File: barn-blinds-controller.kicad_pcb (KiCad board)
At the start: 4 copper layers, 65 x 60 mm, 85 parts, among them J1 DC005-T20, J2 KH-TYPE-C-16P (Kinghelm), J3 Conn_01x08, J4 Conn_01x05, SW1 RESET, SW2 BOOT, U1 DCDC Converter, U10 TMP235, U11 ACS723xLCTR-05AB, U2 AP2112K-3.3, U3 ESP32-S3-WROOM-1, U4 ISO7760DBQ, U5 ISO7760DBQ, U6 ISO7760DBQ, U7 AMS1117-3.3, U8 TB6612FNG, U9 TB6612FNG

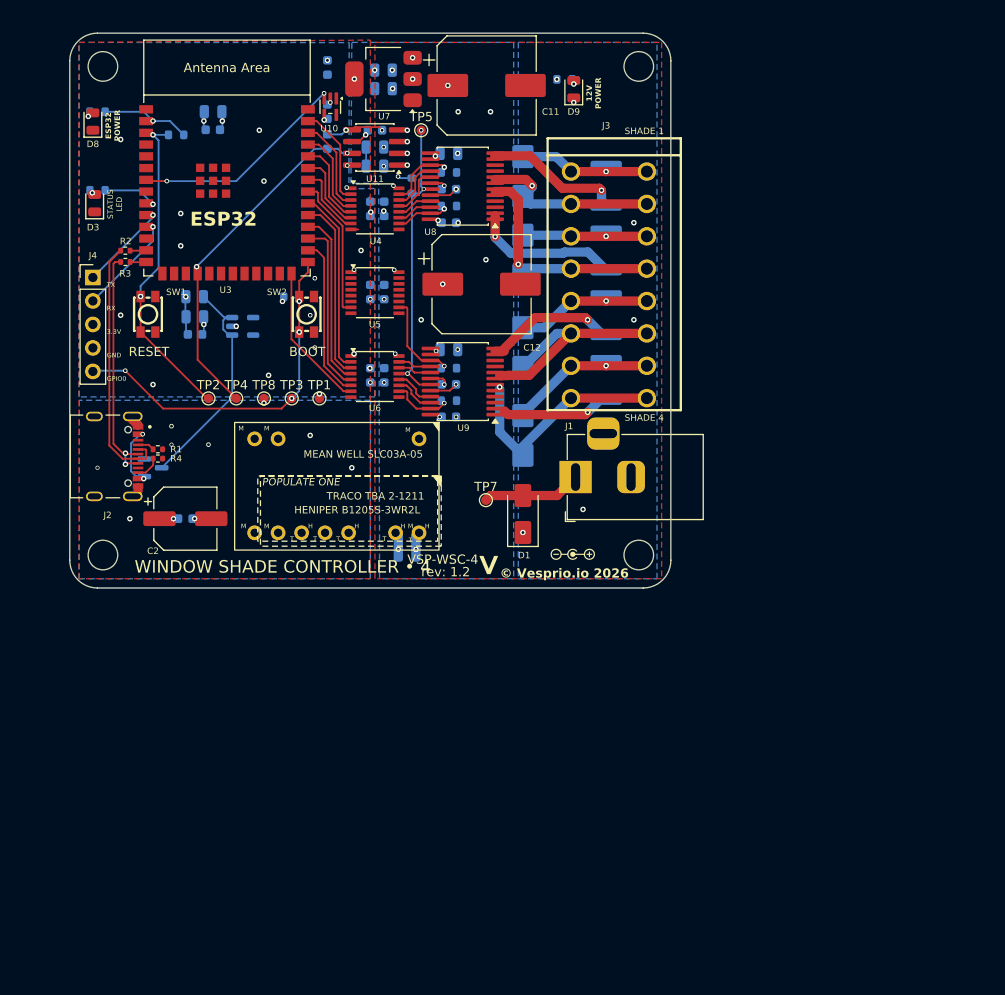
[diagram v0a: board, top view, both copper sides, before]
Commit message: Updating routing with new terminal block
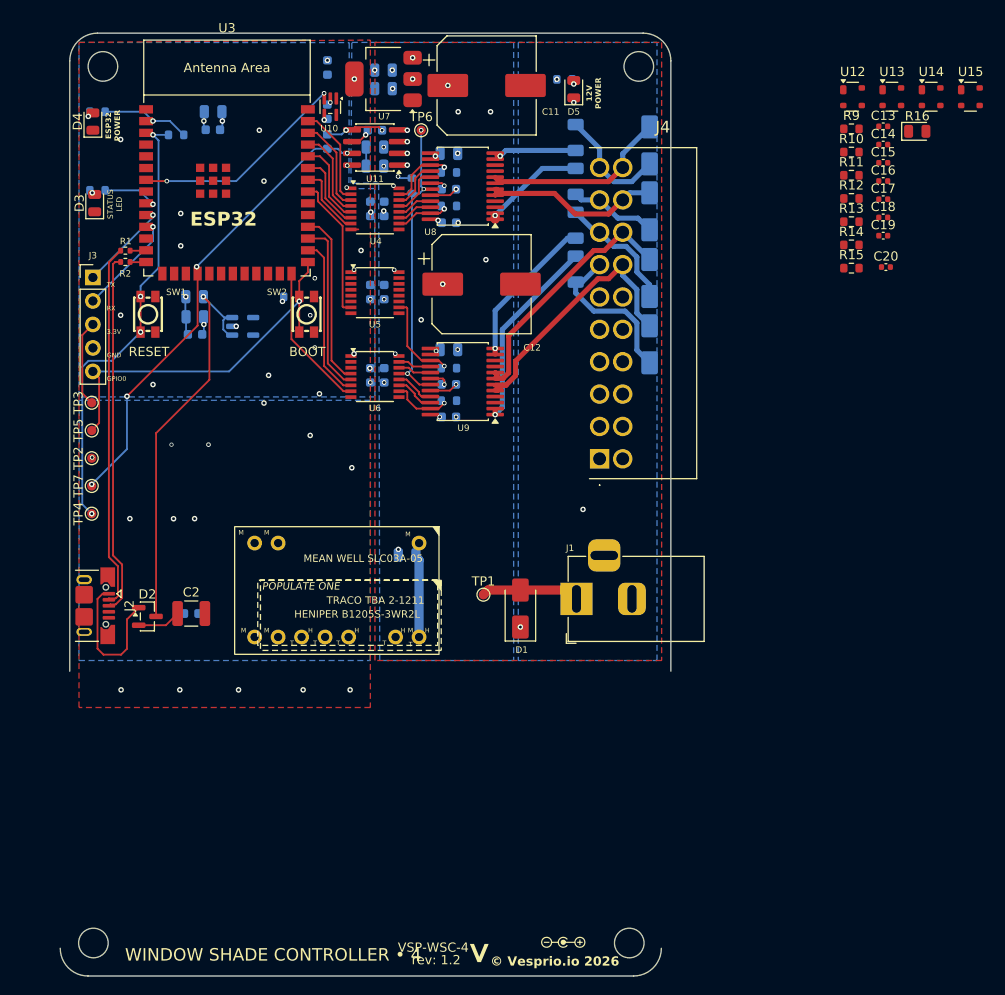
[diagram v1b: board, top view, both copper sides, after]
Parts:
- removed the J3 at (135.3, 76.2)
- removed the R1 at (86.5, 94.0)
- removed the R4 at (86.5, 95.0)
- added C13: 100nF, Capacitor_SMD:C_0402_1005Metric, F.Cu at (165.0, 59.1)
- added C14: 100nF, Capacitor_SMD:C_0402_1005Metric, F.Cu at (165.0, 61.0)
- added C15: 100nF, Capacitor_SMD:C_0402_1005Metric, F.Cu at (165.0, 63.0)
- added C16: 100nF, Capacitor_SMD:C_0402_1005Metric, F.Cu at (165.0, 65.0)
- added C17: 100nF, Capacitor_SMD:C_0402_1005Metric, F.Cu at (165.0, 67.0)
- added C18: 100nF, Capacitor_SMD:C_0402_1005Metric, F.Cu at (165.0, 68.9)
- added C19: 100nF, Capacitor_SMD:C_0402_1005Metric, F.Cu at (165.0, 70.9)
- added C20: 100nF, Capacitor_SMD:C_0402_1005Metric, F.Cu at (165.3, 74.3)
- added J4: Phoenix Contact 1786918, barn_shade_controller:Phoenix Contact 1786918, F.Cu at (134.3, 95.0)
- added R10: 10k, Resistor_SMD:R_0603_1608Metric, F.Cu at (161.5, 61.9)
- added R11: 10k, Resistor_SMD:R_0603_1608Metric, F.Cu at (161.5, 64.4)
- added R12: 10k, Resistor_SMD:R_0603_1608Metric, F.Cu at (161.5, 66.9)
- added R13: 10k, Resistor_SMD:R_0603_1608Metric, F.Cu at (161.5, 69.4)
- added R14: 10k, Resistor_SMD:R_0603_1608Metric, F.Cu at (161.5, 71.9)
- added R15: 10k, Resistor_SMD:R_0603_1608Metric, F.Cu at (161.5, 74.4)
- added R16: 10k, Diode_SMD:D_0805_2012Metric, F.Cu at (168.6, 59.6)
- added R9: 10k, Resistor_SMD:R_0603_1608Metric, F.Cu at (161.5, 59.4)
- added U12: PRTR5V0U2X, Package_TO_SOT_SMD:SOT-143, F.Cu at (161.6, 55.9)
- added U13: PRTR5V0U2X, Package_TO_SOT_SMD:SOT-143, F.Cu at (165.9, 55.9)
- added U14: PRTR5V0U2X, Package_TO_SOT_SMD:SOT-143, F.Cu at (170.1, 55.9)
- added U15: PRTR5V0U2X, Package_TO_SOT_SMD:SOT-143, F.Cu at (174.4, 55.9)
- C2: value 100uF -> 100uF 10V; footprint Capacitor_SMD:CP_Elec_6.3x5.4 -> Capacitor_SMD:C_1210_3225Metric
- D2: moved to F.Cu
- D3: footprint PCM_JLCPCB:D_0805 -> Diode_SMD:D_0805_2012Metric
- D4: renamed from D8; footprint PCM_JLCPCB:D_0805 -> Diode_SMD:D_0805_2012Metric
- D6: renamed from D4; value SMBJ15CA -> SMAJ15CA; footprint PCM_JLCPCB:D_SMB -> Diode_SMD:D_SMA
- D7: value SMBJ15CA -> SMAJ15CA; footprint PCM_JLCPCB:D_SMB -> Diode_SMD:D_SMA
- D8: renamed from D5; value SMBJ15CA -> SMAJ15CA; footprint PCM_JLCPCB:D_SMB -> Diode_SMD:D_SMA
- D9: renamed from D6; value SMBJ15CA -> SMAJ15CA; footprint PCM_JLCPCB:D_SMB -> Diode_SMD:D_SMA
- F1, F2, F3, F4: value Polyfuse mSMD110 -> Polyfuse 1206L110/16NR; footprint Fuse:Fuse_1812_4532Metric -> Fuse:Fuse_1206_3216Metric
- J2: value KH-TYPE-C-16P (Kinghelm) -> USB_B_Micro; footprint barn_shade_controller:KINGHELM_KH-TYPE-C-16P -> Connector_USB:USB_Micro-B_XKB_U254-051T-4BH83-F1S
- TP1: renamed from TP7; footprint barn_shade_controller:TestPoint_Pad_D1.0mm_No_SolderMask -> TestPoint:TestPoint_Pad_D1.0mm
- TP2: renamed from TP8; footprint barn_shade_controller:TestPoint_Pad_D1.0mm_No_SolderMask -> TestPoint:TestPoint_Pad_D1.0mm
- TP3: renamed from TP1; footprint barn_shade_controller:TestPoint_Pad_D1.0mm_No_SolderMask -> TestPoint:TestPoint_Pad_D1.0mm
- TP4: renamed from TP2; footprint barn_shade_controller:TestPoint_Pad_D1.0mm_No_SolderMask -> TestPoint:TestPoint_Pad_D1.0mm
- TP5: renamed from TP3; footprint barn_shade_controller:TestPoint_Pad_D1.0mm_No_SolderMask -> TestPoint:TestPoint_Pad_D1.0mm
- TP6: renamed from TP5; footprint barn_shade_controller:TestPoint_Pad_D1.0mm_No_SolderMask -> TestPoint:TestPoint_Pad_D1.0mm
- TP7: renamed from TP4; footprint barn_shade_controller:TestPoint_Pad_D1.0mm_No_SolderMask -> TestPoint:TestPoint_Pad_D1.0mm
- U3: footprint PCM_Espressif:ESP32-S3-WROOM-1 -> Espressif:ESP32-S3-WROOM-1
- moved H3 42.0 mm to (137.5, 147.4)
- moved H4 42.0 mm to (79.6, 147.4)
- moved D7 34.2 mm to (139.7, 61.1), turned to -90 degrees
- moved F4 26.4 mm to (131.7, 60.3)
- moved TP3 24.6 mm to (79.4, 89.0), turned to 90 degrees
- moved D6 22.7 mm to (139.7, 82.6), turned to 90 degrees
- moved TP5 21.9 mm to (79.4, 92.0), turned to 90 degrees
- moved D9 20.1 mm to (139.7, 68.3), turned to -90 degrees
- moved TP2 19.7 mm to (79.4, 95.0), turned to 90 degrees
- moved TP7 18.3 mm to (79.4, 98.0), turned to 90 degrees
- moved TP4 17.7 mm to (79.4, 101.0), turned to 90 degrees
- moved J2 16.2 mm to (78.9, 110.9)
- moved D2 16.1 mm to (85.4, 112.1)
- moved F3 14.8 mm to (131.7, 65.0), turned to 90 degrees
- moved D8 13.9 mm to (139.7, 75.5), turned to -90 degrees
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- renumbered D9 to D5, J4 to J3, R2 to R1, R3 to R2, R5 to R3, R6 to R4, R7 to R5, R8 to R6, R9 to R7, R10 to R8
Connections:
- net /ACS723 renamed ACS723
- net /ISO_M1_CLOSE renamed ISO_SH4_CLOSE
- net /ISO_M1_OPEN renamed ISO_SH4_OPEN
- net /ISO_M2_CLOSE renamed ISO_SH3_CLOSED
- net /ISO_M2_OPEN renamed ISO_SH3_OPEN
- net /ISO_PWM_M1 renamed ISO_SH4_PWM
- net /ISO_PWM_M2 renamed ISO_SH3_PWM
- net /ISO_PWM_M3 renamed ISO_SH2_PWM
- net /ISO_PWM_M4 renamed ISO_SH1_PWM
- net /ISO_STBY renamed ISO_STBY
- net /M1_AIN1 renamed SH4_IN1
- net /M1_AIN2 renamed SH4_IN2
- net /M2_BIN1 renamed SH3_IN1
- net /M2_BIN2 renamed SH3_IN2
- net /M3_AIN1 renamed SH2_IN1
- net /M3_AIN2 renamed SH2_IN2
- net /M4_BIN1 renamed SH1_IN1
- net /M4_BIN2 renamed SH1_IN2
- net /PWM_M1 renamed SH4_PWM
- net /PWM_M2 renamed SH3_PWM
- net /PWM_M3 renamed SH2_PWM
- net /PWM_M4 renamed SH1_PWM
- net /STBY renamed STBY
- net /TMP235 renamed TMP235
- net /USB_DN renamed USB_DN
- net /USB_DP renamed USB_DP
- net Net-(D4-Pad1) renamed SHADE1_UP
- net Net-(D6-Pad2) renamed SHADE3_UP
- net Net-(D7-Pad2) renamed SHADE4_UP
- D2 pad 1: VBUS -> Net-(J2-VBUS)
- D6 pad 2: U2_B02 -> SHADE1_DOWN
- D7 pad 1: U3_A02 -> SHADE4_DOWN
- D8 pad 1: U2_A02 -> SHADE2_DOWN
- D8 pad 2: Net-(D5-Pad2) (its old number) -> SHADE2_UP
- D9 pad 1: U3_B02 -> SHADE3_DOWN
- F1 pad 1: U2_B01 -> SHADE1_UP_FUSED
- F2 pad 1: U2_A01 -> SHADE2_UP_FUSED
- F2 pad 2: Net-(D5-Pad2) (its old number) -> SHADE2_UP
- F3 pad 2: U3_B01 -> SHADE3_UP_FUSED
- F4 pad 1: U3_A01 -> SHADE4_UP_FUSED
- R1 pad 1: /USB-C and 5V Diode-OR/DN -> USB_IN_DN
- R2 pad 1: /USB-C and 5V Diode-OR/DP -> USB_IN_DP
- U3 pad 28: /ISO_M3_CLOSE -> ISO_SH2_CLOSED
- U3 pad 29: /ISO_M3_OPEN -> ISO_SH2_OPEN
- U3 pad 31: /ISO_M4_OPEN -> ISO_SH2_OPEN
- U3 pad 32: /ISO_M4_CLOSE -> ISO_SH2_CLOSED
- U6 pad 2: /ISO_M4_CLOSE -> ISO_SH1_CLOSED
- U6 pad 3: /ISO_M4_OPEN -> ISO_SH1_OPEN
- U6 pad 5: /ISO_M3_OPEN -> ISO_SH2_OPEN
- U6 pad 6: /ISO_M3_CLOSE -> ISO_SH2_CLOSED
- U8 pad 1: U2_A01 -> SHADE3_UP_FUSED
- U8 pad 11: U2_B01 -> SHADE4_UP_FUSED
- U8 pad 12: U2_B01 -> SHADE4_UP_FUSED
- U8 pad 2: U2_A01 -> SHADE3_UP_FUSED
- U8 pad 5: U2_A02 -> SHADE3_DOWN
- U8 pad 6: U2_A02 -> SHADE3_DOWN
- U8 pad 7: U2_B02 -> SHADE4_DOWN
- U8 pad 8: U2_B02 -> SHADE4_DOWN
- U9 pad 1: U3_A01 -> SHADE1_UP_FUSED
- U9 pad 11: U3_B01 -> SHADE2_UP_FUSED
- U9 pad 12: U3_B01 -> SHADE2_UP_FUSED
- U9 pad 2: U3_A01 -> SHADE1_UP_FUSED
- U9 pad 5: U3_A02 -> SHADE1_DOWN
- U9 pad 6: U3_A02 -> SHADE1_DOWN
- U9 pad 7: U3_B02 -> SHADE2_DOWN
- U9 pad 8: U3_B02 -> SHADE2_DOWN
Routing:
- net USB_IN_DN: track 0.00 -> 39.5 mm
- net USB_IN_DP: track 0.00 -> 39.2 mm
- net SHADE1_DOWN: track 0.00 -> 29.3 mm
- net /USB-C and 5V Diode-OR/DN: track 28.0 -> 0.00 mm
- net SHADE2_DOWN: track 0.00 -> 27.5 mm
- net /USB-C and 5V Diode-OR/DP: track 26.1 -> 0.00 mm, vias 2 -> 0
- net U3_B02: track 24.5 -> 0.00 mm
- net U3_A02: track 23.7 -> 0.00 mm, vias 1 -> 0
- net U2_A02: track 23.2 -> 0.00 mm, vias 1 -> 0
- net SHADE1_UP_FUSED: track 0.00 -> 21.2 mm, vias 0 -> 1
- net SHADE4_DOWN: track 0.00 -> 20.2 mm
- net +5V_OR: track 24.5 -> 44.2 mm, vias 0 -> 1
- net /ISO_M4_OPEN: track 19.7 -> 0.00 mm
- net U2_B02: track 19.6 -> 0.00 mm, vias 1 -> 0
- net SHADE3_DOWN: track 0.00 -> 19.3 mm
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- added copper zone on In2.Cu, net GND_ISO
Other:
- board size 65 x 60 mm -> 66 x 102 mm
- board text removed: "SHADE 1"
- board text removed: "SHADE 4"

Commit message: Adding switches to PCB
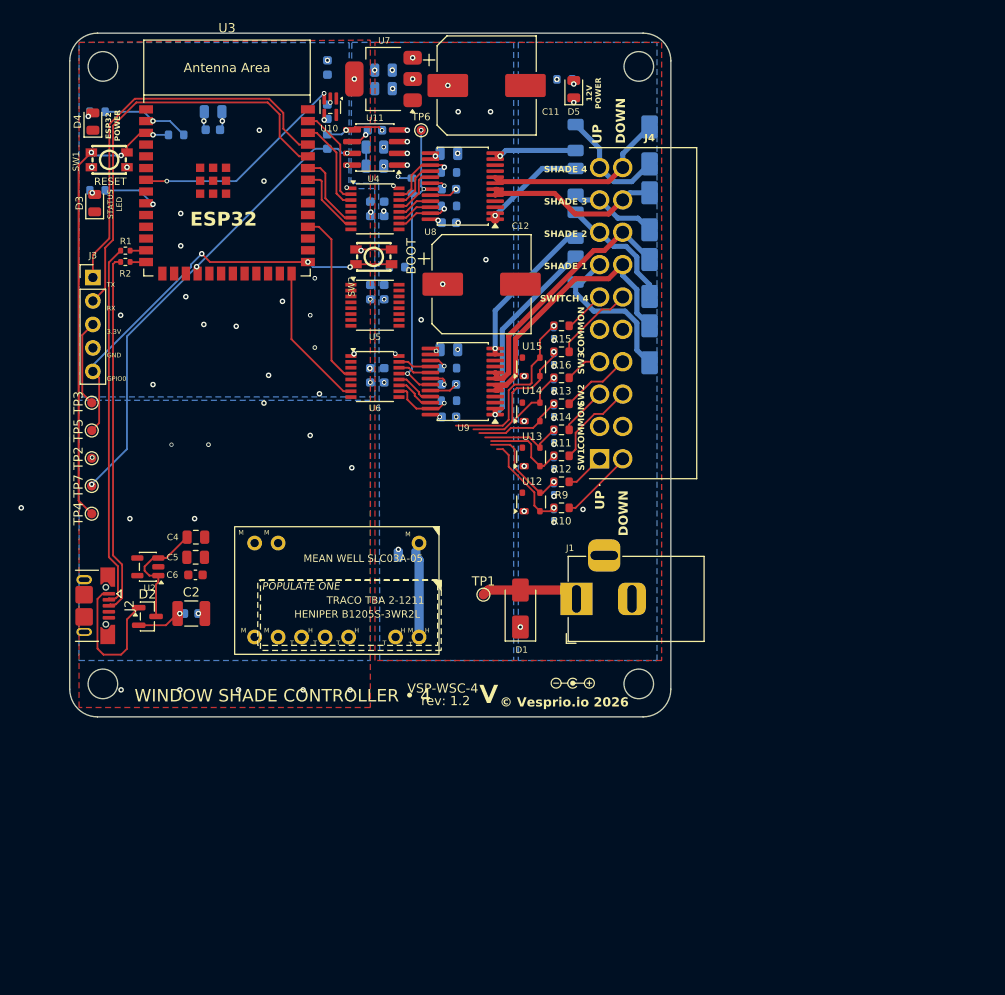
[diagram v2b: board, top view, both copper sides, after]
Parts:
- C13, C14, C15, C16, C17, C18, C19, C20: moved to B.Cu
- C4, C5, C6, U2: moved to F.Cu
- R16: footprint Diode_SMD:D_0805_2012Metric -> Resistor_SMD:R_0603_1608Metric
- moved U12 55.9 mm to (126.9, 99.7), turned to 90 degrees
- moved U15 55.8 mm to (126.9, 85.1), turned to 90 degrees
- moved U13 55.1 mm to (126.9, 94.8), turned to 90 degrees
- moved U14 55.1 mm to (126.9, 90.0), turned to 90 degrees
- moved C14 53.6 mm to (129.3, 101.1), turned to -90 degrees
- moved C13 53.0 mm to (129.3, 98.3), turned to -90 degrees
- moved R10 49.6 mm to (130.2, 100.3), turned to 180 degrees
- moved R9 49.4 mm to (130.2, 97.5), turned to 180 degrees
- moved C16 46.9 mm to (129.3, 95.5), turned to -90 degrees
- moved C15 46.4 mm to (129.3, 92.7), turned to -90 degrees
- moved R16 45.3 mm to (130.2, 83.5), turned to 180 degrees
- moved R12 41.9 mm to (130.2, 94.7), turned to 180 degrees
- moved R11 41.7 mm to (130.2, 91.9), turned to 180 degrees
- moved C18 41.3 mm to (129.3, 89.9), turned to -90 degrees
- moved C17 40.9 mm to (129.3, 87.1), turned to -90 degrees
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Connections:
- C13 pad 1: GPIO4 -> SW1_UP_IN
- C14 pad 1: GPIO5 -> SW1_DOWN_IN
- C15 pad 1: GPIO6 -> SW2_UP_IN
- C16 pad 1: GPIO8 -> SW2_DOWN_IN
- C17 pad 1: GPIO9 -> SW3_UP_IN
- C18 pad 1: GPIO11 -> SW3_DOWN_IN
- C19 pad 1: GPIO12 -> SW4_UP_IN
- C20 pad 1: GPIO13 -> SW4_DOWN_IN
- J3 pad 1: Net-(J3-Pin_1) -> U0TXD
- J3 pad 2: Net-(J3-Pin_2) -> U0RXD
- R10 pad 2: GPIO5 -> SW1_DOWN_IN
- R11 pad 2: GPIO6 -> SW2_UP_IN
- R12 pad 2: GPIO8 -> SW2_DOWN_IN
- R13 pad 2: GPIO9 -> SW3_UP_IN
- R14 pad 2: GPIO11 -> SW3_DOWN_IN
- R15 pad 2: GPIO12 -> SW4_UP_IN
- R16 pad 2: GPIO13 -> SW4_DOWN_IN
- R9 pad 2: GPIO4 -> SW1_UP_IN
- U12 pad 2: GPIO5 -> SW1_DOWN_IN
- U12 pad 3: GPIO4 -> SW1_UP_IN
- U13 pad 2: GPIO8 -> SW2_DOWN_IN
- U13 pad 3: GPIO6 -> SW2_UP_IN
- U14 pad 2: GPIO11 -> SW3_DOWN_IN
- U14 pad 3: GPIO9 -> SW3_UP_IN
- U15 pad 2: GPIO13 -> SW4_DOWN_IN
- U15 pad 3: GPIO12 -> SW4_UP_IN
- U3 pad 10: Net-(J3-Pin_1) -> unconnected-(U3-GPIO17/U1TXD/ADC2_CH6-Pad10)
- U3 pad 11: Net-(J3-Pin_2) -> unconnected-(U3-GPIO18/U1RXD/ADC2_CH7/CLK_OUT3-Pad11)
- U3 pad 12: unconnected-(U3-GPIO8/TOUCH8/ADC1_CH7/SUBSPICS1-Pad12) -> SW2_DOWN_IN
- U3 pad 15: unconnected-(U3-GPIO3/TOUCH3/ADC1_CH2-Pad15) -> ISO_SH4_OPEN
- U3 pad 17: unconnected-(U3-GPIO9/TOUCH9/ADC1_CH8/FSPIHD/SUBSPIHD-Pad17) -> SW3_UP_IN
- U3 pad 19: unconnected-(U3-GPIO11/TOUCH11/ADC2_CH0/FSPID/FSPIIO5/SUBSPID-Pad19) -> SW3_DOWN_IN
- U3 pad 20: unconnected-(U3-GPIO12/TOUCH12/ADC2_CH1/FSPICLK/FSPIIO6/SUBSPICLK-Pad20) -> SW4_UP_IN
- U3 pad 21: unconnected-(U3-GPIO13/TOUCH13/ADC2_CH2/FSPIQ/FSPIIO7/SUBSPIQ-Pad21) -> SW4_DOWN_IN
- U3 pad 23: unconnected-(U3-GPIO21-Pad23) -> ISO_SH3_OPEN
- U3 pad 28: ISO_SH2_CLOSED -> ISO_SH1_CLOSED
- U3 pad 29: ISO_SH2_OPEN -> ISO_SH1_OPEN
- U3 pad 36: ISO_SH4_OPEN -> U0RXD
- U3 pad 37: ISO_SH3_OPEN -> U0TXD
- U3 pad 4: unconnected-(U3-GPIO4/TOUCH4/ADC1_CH3-Pad4) -> SW1_UP_IN
- U3 pad 5: unconnected-(U3-GPIO5/TOUCH5/ADC1_CH4-Pad5) -> SW1_DOWN_IN
- U3 pad 6: unconnected-(U3-GPIO6/TOUCH6/ADC1_CH5-Pad6) -> SW2_UP_IN
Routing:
- net U0RXD: track 0.00 -> 45.8 mm
- net U0TXD: track 0.00 -> 43.0 mm
- net +5V_OR: track 44.2 -> 12.6 mm, vias 1 -> 0
- net SW4_UP_IN: track 0.00 -> 19.2 mm, vias 0 -> 1
- net ISO_SH2_OPEN: track 18.7 -> 0.00 mm
- net ISO_SH2_CLOSED: track 17.6 -> 0.00 mm
- net ISO_SH1_PWM: track 15.5 -> 0.00 mm
- net SW4_DOWN_IN: track 0.00 -> 14.9 mm, vias 0 -> 1
- net Net-(J3-Pin_2): track 10.7 -> 0.00 mm, vias 1 -> 0
- net SW1_DOWN_IN: track 0.00 -> 10.7 mm, vias 0 -> 1
- net SW1_UP_IN: track 0.00 -> 10.6 mm, vias 0 -> 1
- net ISO_SH3_OPEN: track 9.72 -> 0.00 mm
- net SW2_DOWN: track 0.00 -> 9.61 mm
- net SW3_DOWN_IN: track 0.00 -> 9.59 mm, vias 0 -> 1
- net Net-(J3-Pin_1): track 9.44 -> 0.00 mm, vias 1 -> 0
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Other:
- board size 66 x 102 mm -> 65 x 73.9 mm
- board text added: "COMMON"
- board text added: "DOWN"
- board text added: "SHADE 1"
- board text added: "SHADE 2"
- board text added: "SHADE 3"
- board text added: "SHADE 4"
- board text added: "SW1"
- board text added: "SW2"
- board text added: "SW3"
- board text added: "SWITCH 4"
- board text added: "UP"

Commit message: Completed added switch circuits
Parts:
- moved C1 1.89 mm to (113.5, 107.3)
- moved U15 0.64 mm to (126.9, 85.7)
- moved C_ISO_C1 0.51 mm to (109.0, 77.0)
- moved C_ISO_D1 0.51 mm to (110.5, 77.0)
- moved SW1 0.14 mm to (81.1, 62.7)
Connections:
- U3 pad 12: SW2_DOWN_IN -> unconnected-(U3-GPIO8/TOUCH8/ADC1_CH7/SUBSPICS1-Pad12)
- U3 pad 15: ISO_SH4_OPEN -> SW1_DOWN_IN
- U3 pad 16: unconnected-(U3-GPIO46-Pad16) -> SW1_UP_IN
- U3 pad 17: SW3_UP_IN -> SW2_DOWN_IN
- U3 pad 18: ACS723 -> SW2_UP_IN
- U3 pad 20: SW4_UP_IN -> SW3_UP_IN
- U3 pad 22: unconnected-(U3-GPIO14/TOUCH14/ADC2_CH3/FSPIWP/FSPIDQS/SUBSPIWP-Pad22) -> SW4_UP_IN
- U3 pad 23: ISO_SH3_OPEN -> ISO_SH2_PWM
- U3 pad 24: unconnected-(U3-GPIO47/SPICLK_P/SUBSPICLK_P_DIFF-Pad24) -> ISO_SH2_CLOSED
- U3 pad 25: unconnected-(U3-GPIO48/SPICLK_N/SUBSPICLK_N_DIFF-Pad25) -> ISO_SH2_OPEN
- U3 pad 26: ISO_SH2_PWM -> unconnected-(U3-GPIO45-Pad26)
- U3 pad 28: ISO_SH1_CLOSED -> ISO_STBY
- U3 pad 30: ISO_STBY -> ISO_SH1_CLOSED
- U3 pad 31: ISO_SH2_OPEN -> ISO_SH1_PWM
- U3 pad 32: ISO_SH2_CLOSED -> ISO_SH4_PWM
- U3 pad 33: ISO_SH1_PWM -> ISO_SH4_CLOSE
- U3 pad 34: ISO_SH4_PWM -> ISO_SH4_OPEN
- U3 pad 35: ISO_SH4_CLOSE -> ISO_SH3_OPEN
- U3 pad 4: SW1_UP_IN -> TMP235
- U3 pad 5: SW1_DOWN_IN -> ACS723
- U3 pad 6: SW2_UP_IN -> unconnected-(U3-GPIO6/TOUCH6/ADC1_CH5-Pad6)
- U3 pad 7: TMP235 -> unconnected-(U3-GPIO7/TOUCH7/ADC1_CH6-Pad7)
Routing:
- net SW1_DOWN_IN: track 10.7 -> 56.2 mm
- net SW1_UP_IN: track 10.6 -> 54.7 mm
- net SW2_DOWN_IN: track 9.22 -> 52.7 mm
- net SW3_UP_IN: track 7.09 -> 48.7 mm
- net SW2_UP_IN: track 8.94 -> 49.8 mm
- net SW3_DOWN_IN: track 9.59 -> 48.3 mm
- net SW4_DOWN_IN: track 14.9 -> 48.8 mm
- net SW4_UP_IN: track 19.2 -> 49.7 mm
- net ISO_SH1_CLOSED: track 0.00 -> 18.0 mm
- net ISO_SH1_OPEN: track 0.00 -> 16.9 mm
- net GND_ISO: track 11.7 -> 28.5 mm, vias 46 -> 55
- net ISO_SH2_CLOSED: track 0.00 -> 16.5 mm
- net ISO_SH2_OPEN: track 0.00 -> 15.4 mm
- net ISO_SH1_PWM: track 0.00 -> 15.0 mm
- net ACS723: track 50.1 -> 63.4 mm
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
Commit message: Version bump
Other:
- board text added: "rev: 1.3"
- board text removed: "rev: 1.2"
